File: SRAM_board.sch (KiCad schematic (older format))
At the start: 78 parts, among them J1 JP3, J10 Optional Interrupt Pins, J11 Optional Interrupt Pin, J12 GPIO 1, J13 GPIO 0, J14 USB_OTG, J2 JP6, J3 JP2, J4 JP5, J5 Screw_Terminal_01x09, J6 Screw_Terminal_01x06, J7 Optional I2C/UART, J9 Optional Interrupt Pin, SW1 KEY1, SW2 KEY0, U1 LD1085D2T33R, U2 MS561101BA03-50, U3 IIS2MDCTR, U4 GS832032AGT-150I, U5 BMI055, U6 ICM-20689, U7 FT232RL

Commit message: cleanup
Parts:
- removed unit 2 of U4
- removed unit 3 of U4
- removed unit 4 of U4
- removed unit 5 of U4
- removed unit 6 of U4
- added U? (x5): DE10_SRAM_expansion_GS832032AGT-150I-DE10_SRAM_ex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, symbol DE10_SRAM_expansion:DE10_SRAM_expansion_GS832032AGT-150I-DE10_SRAM_expansion
- U1: symbol SRAM_board-rescue:DE10_SRAM_expansion_LD1085D2T33R-DE10_SRAM_expansion -> DE10_SRAM_expansion:DE10_SRAM_expansion_LD1085D2T33R-DE10_SRAM_expansion
- U2: symbol SRAM_board-rescue:DE10_SRAM_expansion_MS561101BA03-50-DE10_SRAM_expansion -> DE10_SRAM_expansion:DE10_SRAM_expansion_MS561101BA03-50-DE10_SRAM_expansion
- U3: symbol SRAM_board-rescue:DE10_SRAM_expansion_IIS2MDCTR-DE10_SRAM_expansion -> DE10_SRAM_expansion:DE10_SRAM_expansion_IIS2MDCTR-DE10_SRAM_expansion
- U4: symbol SRAM_board-rescue:DE10_SRAM_expansion_GS832032AGT-150I-DE10_SRAM_expansion -> DE10_SRAM_expansion:DE10_SRAM_expansion_GS832032AGT-150I-DE10_SRAM_expansion
- U5: symbol SRAM_board-rescue:DE10_SRAM_expansion_BMI055-DE10_SRAM_expansion -> DE10_SRAM_expansion:DE10_SRAM_expansion_BMI055-DE10_SRAM_expansion
- U6: symbol SRAM_board-rescue:DE10_SRAM_expansion_ICM-20689-DE10_SRAM_expansion -> DE10_SRAM_expansion:DE10_SRAM_expansion_ICM-20689-DE10_SRAM_expansion
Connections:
- net A0: now also U?.37 (A0)
- net A1: now also U?.36 (A1)
- net A10: now also U?.43 (A)
- net A11: now also U?.45 (A)
- net A12: now also U?.47 (A)
- net A13: now also U?.48 (A)
- net A14: now also U?.49 (A)
- net A15: now also U?.50 (A)
- net A16: now also U?.81 (A)
- net A17: now also U?.82 (A)
- net A18: now also U?.99 (A)
- net A19: now also U?.100 (A)
- net A2: now also U?.32 (A)
- net A3: now also U?.33 (A)
- net A4: now also U?.34 (A)
- net A5: now also U?.35 (A)
- net A6: now also U?.39 (A)
- net A7: now also U?.44 (A)
- net A8: now also U?.42 (A)
- net A9: now also U?.46 (A)
- net CLK: now also U?.89 (CLK)
- net DQA1: now also U?.52 (DQA)
- net DQA2: now also U?.53 (DQA)
- net DQA3: now also U?.56 (DQA)
- net DQA4: now also U?.57 (DQA)
- net DQA5: now also U?.58 (DQA)
- net DQA6: now also U?.59 (DQA)
- net DQA7: now also U?.62 (DQA)
- net DQA8: now also U?.63 (DQA)
- net DQB1: now also U?.79 (DQB)
- net DQB2: now also U?.78 (DQB)
- net DQB3: now also U?.75 (DQB)
- net DQB4: now also U?.74 (DQB)
- net DQB5: now also U?.73 (DQB)
- net DQB6: now also U?.72 (DQB)
- net DQB7: now also U?.69 (DQB)
- net DQB8: now also U?.68 (DQB)
- net DQC1: now also U?.2 (DQC)
- net DQC2: now also U?.3 (DQC)
- net DQC3: now also U?.6 (DQC)
- net DQC4: now also U?.7 (DQC)
- net DQC5: now also U?.8 (DQC)
- net DQC6: now also U?.9 (DQC)
- net DQC7: now also U?.12 (DQC)
- net DQC8: now also U?.13 (DQC)
- net DQD1: now also U?.18 (DQD)
- net DQD2: now also U?.19 (DQD)
- net DQD3: now also U?.22 (DQD)
- net DQD4: now also U?.23 (DQD)
- net DQD5: now also U?.24 (DQD)
- net DQD6: now also U?.25 (DQD)
- net DQD7: now also U?.28 (DQD)
- net DQD8: now also U?.29 (DQD)
- net DQPA: now also U?.51 (DQPA)
- net DQPB: now also U?.80 (DQPB)
- net DQPC: now also U?.1 (DQPC)
- net DQPD: now also U?.30 (DQPD)
- net ZZ: now also U?.64 (ZZ)
- net ~ADSC: now also U?.85 (~ADSC)
- net ~ADSP: now also U?.84 (~ADSP)
- net ~ADV: now also U?.83 (~ADV)
- net ~BA: now also U?.93 (~BA)
- net ~BB: now also U?.94 (~BB)
- net ~BC: now also U?.95 (~BC)
- net ~BD: now also U?.96 (~BD)
- net ~BW: now also U?.87 (~BW)
- net ~E1: now also U?.98 (~E1)
- net ~E2: now also U?.97 (~E2)
- net ~E3: now also U?.92 (~E3)
- net ~FT: now also U?.14 (~FT)
- net ~G: now also U?.86 (~G)
- net ~GW: now also U?.88 (~GW)
- net ~LBO: now also U?.31 (~LBO)
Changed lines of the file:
@@
 EESchema Schematic File Version 4
-LIBS:SRAM_board-cache
 EELAYER 30 0
 EELAYER END
@@
 GP Buttons, Leds\n
 $Comp
-L SRAM_board-rescue:DE10_SRAM_expansion_BMI055-DE10_SRAM_expansion U5
+L DE10_SRAM_expansion:DE10_SRAM_expansion_BMI055-DE10_SRAM_expansion U5
 U 1 1 5DD1283D
 P 10400 7500
@@
 $EndComp
 $Comp
-L SRAM_board-rescue:DE10_SRAM_expansion_LD1085D2T33R-DE10_SRAM_expansion U1
+L DE10_SRAM_expansion:DE10_SRAM_expansion_LD1085D2T33R-DE10_SRAM_expansion U1
 U 1 1 5DD15E38
 P 4050 1850
@@
 $EndComp
 $Comp
-L SRAM_board-rescue:DE10_SRAM_expansion_GS832032AGT-150I-DE10_SRAM_expansion U4
+L DE10_SRAM_expansion:DE10_SRAM_expansion_GS832032AGT-150I-DE10_SRAM_expansion U4
 U 1 1 5DD17A72
 P 6000 4600
@@
 $EndComp
 $Comp
-L SRAM_board-rescue:DE10_SRAM_expansion_GS832032AGT-150I-DE10_SRAM_expansion U4
-U 2 1 5DD1E8B0
-P 18200 2150
-F 0 "U4" H 17900 2950 50  0000 C CNN
-F 1 "GS832032AGT-150I" H 18200 800 50  0000 C CNN
-F 2 "DE10_SRAM_board:PQFP-100_14x20mm_P0.65mm" H 17950 150 50  0001 C CNN
-F 3 "" H 17850 250 50  0001 C CNN
-	2    18200 2150
-	1    0    0    -1
-$EndComp
-$Comp
-L SRAM_board-rescue:DE10_SRAM_expansion_GS832032AGT-150I-DE10_SRAM_expansion U4
-U 3 1 5DD336C8
-P 14750 2000
-F 0 "U4" H 14650 2850 50  0000 L CNN
-F 1 "GS832032AGT-150I" H 14650 1650 50  0000 L CNN
-F 2 "DE10_SRAM_board:PQFP-100_14x20mm_P0.65mm" H 14500 0   50  0001 C CNN
-F 3 "" H 14400 100 50  0001 C CNN
-	3    14750 2000
-	1    0    0    -1
-$EndComp
-$Comp
-L SRAM_board-rescue:DE10_SRAM_expansion_GS832032AGT-150I-DE10_SRAM_expansion U4
-U 4 1 5DD38B2E
-P 9450 2000
-F 0 "U4" H 9650 2850 50  0000 L CNN
-F 1 "GS832032AGT-150I" H 8900 1650 50  0000 L CNN
-F 2 "DE10_SRAM_board:PQFP-100_14x20mm_P0.65mm" H 9200 0   50  0001 C CNN
-F 3 "" H 9100 100 50  0001 C CNN
-	4    9450 2000
-	-1   0    0    -1
-$EndComp
-$Comp
-L SRAM_board-rescue:DE10_SRAM_expansion_GS832032AGT-150I-DE10_SRAM_expansion U4
-U 5 1 5DD3B251
-P 14750 3350
-F 0 "U4" H 15050 4200 50  0000 C CNN
-F 1 "GS832032AGT-150I" H 14750 3100 50  0000 C CNN
-F 2 "DE10_SRAM_board:PQFP-100_14x20mm_P0.65mm" H 14500 1350 50  0001 C CNN
-F 3 "" H 14400 1450 50  0001 C CNN
-	5    14750 3350
-	1    0    0    -1
-$EndComp
-$Comp
-L SRAM_board-rescue:DE10_SRAM_expansion_GS832032AGT-150I-DE10_SRAM_expansion U4
-U 6 1 5DD3D3F0
-P 9450 3250
-F 0 "U4" H 9750 4100 50  0000 C CNN
-F 1 "GS832032AGT-150I" H 9450 3000 50  0000 C CNN
-F 2 "DE10_SRAM_board:PQFP-100_14x20mm_P0.65mm" H 9200 1250 50  0001 C CNN
-F 3 "" H 9100 1350 50  0001 C CNN
-	6    9450 3250
-	-1   0    0    -1
-$EndComp
-$Comp
-L SRAM_board-rescue:DE10_SRAM_expansion_MS561101BA03-50-DE10_SRAM_expansion U2
+L DE10_SRAM_expansion:DE10_SRAM_expansion_MS561101BA03-50-DE10_SRAM_expansion U2
 U 1 1 5DE27368
 P 5750 7600
@@
 $EndComp
 $Comp
-L SRAM_board-rescue:DE10_SRAM_expansion_IIS2MDCTR-DE10_SRAM_expansion U3
+L DE10_SRAM_expansion:DE10_SRAM_expansion_IIS2MDCTR-DE10_SRAM_expansion U3
 U 1 1 5DE29342
 P 5850 10600
@@
 $EndComp
 $Comp
-L SRAM_board-rescue:DE10_SRAM_expansion_ICM-20689-DE10_SRAM_expansion U6
+L DE10_SRAM_expansion:DE10_SRAM_expansion_ICM-20689-DE10_SRAM_expansion U6
 U 1 1 5DE2C4AF
 P 10900 10600
@@
 	17250 10650 17600 10650
 NoConn ~ 17600 10850
+$Comp
+L DE10_SRAM_expansion:DE10_SRAM_expansion_GS832032AGT-150I-DE10_SRAM_expansion U?
+U 4 1 5DEA11D4
+P 9450 2000
+F 0 "U?" H 9517 2965 50  0000 C CNN
+F 1 "DE10_SRAM_expansion_GS832032AGT-150I-DE10_SRAM_expansion" H 9517 2874 50  0000 C CNN
+F 2 "" H 9200 0   50  0001 C CNN
+F 3 "" H 9100 100 50  0001 C CNN
+	4    9450 2000
+	-1   0    0    -1
+$EndComp
+$Comp
+L DE10_SRAM_expansion:DE10_SRAM_expansion_GS832032AGT-150I-DE10_SRAM_expansion U?
+U 6 1 5DEA674C
+P 9450 3250
+F 0 "U?" H 9517 4215 50  0000 C CNN
+F 1 "DE10_SRAM_expansion_GS832032AGT-150I-DE10_SRAM_expansion" H 9517 4124 50  0000 C CNN
+F 2 "" H 9200 1250 50  0001 C CNN
+F 3 "" H 9100 1350 50  0001 C CNN
+	6    9450 3250
+	-1   0    0    -1
+$EndComp
+$Comp
+L DE10_SRAM_expansion:DE10_SRAM_expansion_GS832032AGT-150I-DE10_SRAM_expansion U?
+U 3 1 5DEABA45
+P 14750 2000
+F 0 "U?" H 15128 2296 50  0000 L CNN
+F 1 "DE10_SRAM_expansion_GS832032AGT-150I-DE10_SRAM_expansion" H 15128 2205 50  0000 L CNN
+F 2 "" H 14500 0   50  0001 C CNN
+F 3 "" H 14400 100 50  0001 C CNN
+	3    14750 2000
+	1    0    0    -1
+$EndComp
+$Comp
+L DE10_SRAM_expansion:DE10_SRAM_expansion_GS832032AGT-150I-DE10_SRAM_expansion U?
+U 5 1 5DEAFC8A
+P 14750 3350
+F 0 "U?" H 15128 3696 50  0000 L CNN
+F 1 "DE10_SRAM_expansion_GS832032AGT-150I-DE10_SRAM_expansion" H 15128 3605 50  0000 L CNN
+F 2 "" H 14500 1350 50  0001 C CNN
+F 3 "" H 14400 1450 50  0001 C CNN
+	5    14750 3350
+	1    0    0    -1
+$EndComp
+$Comp
+L DE10_SRAM_expansion:DE10_SRAM_expansion_GS832032AGT-150I-DE10_SRAM_expansion U?
+U 2 1 5DEB5E67
+P 18200 2150
+F 0 "U?" H 18175 3075 50  0000 C CNN
+F 1 "DE10_SRAM_expansion_GS832032AGT-150I-DE10_SRAM_expansion" H 18175 2984 50  0000 C CNN
+F 2 "" H 17950 150 50  0001 C CNN
+F 3 "" H 17850 250 50  0001 C CNN
+	2    18200 2150
+	1    0    0    -1
+$EndComp
 $EndSCHEMATC

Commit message: celanup, I2C improvment, SRAM clock buffer
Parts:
- added C38: 2.2uF, Capacitor_SMD:C_1206_3216Metric_Pad1.42x1.75mm_HandSolder, symbol Device:C_Small
- added C39: 100nF, Capacitor_SMD:C_1206_3216Metric_Pad1.42x1.75mm_HandSolder, symbol Device:C_Small
- added R14, R15, R16: 50R, Resistor_SMD:R_1206_3216Metric_Pad1.42x1.75mm_HandSolder, symbol Device:R_Small
- added U8: CDCLVC1102, DE10_SRAM_board:SOIC-8, symbol DE10_SRAM_expansion:CDCLVC1102
- U4: renamed from U?; value DE10_SRAM_expansion_GS832032AGT-150I-DE10_SRAM_expansion -> GS832032AGT-150I; footprint (none) -> DE10_SRAM_board:PQFP-100_14x20mm_P0.65mm
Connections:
- net +3V3: now also C38.1, C39.1, U8.6 (VDD)
- net CLK: now also R16.1; no longer J13.32 (Pin_32)
- net GND: now also C38.2, C39.2, R15.1, U8.2 (1G), U8.4 (GND)
- new net: R14.1, R15.2, U8.1 (CLKIN)
- new net: R16.2, U8.3 (Y0)
- new net CLK_IN: J13.32 (Pin_32), R14.2
- no-connect marks 21 -> 22
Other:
- note added: "CLOCK BUFFER"
- note added: "This makes the ERC happy\nStill host +5V power"
- note removed: "This makes the ERC happy\nStil host +5V power"
- moved on the sheet: J13, U4B

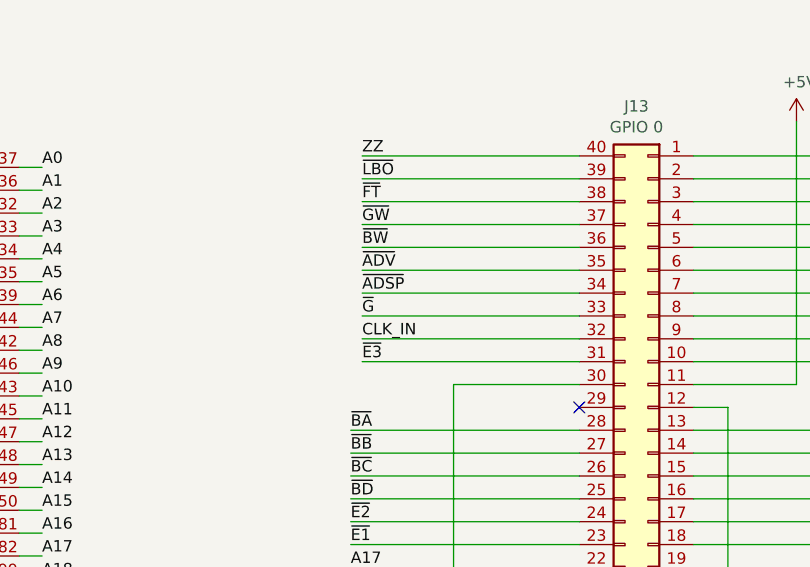
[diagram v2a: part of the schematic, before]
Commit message: switch sram clock pin
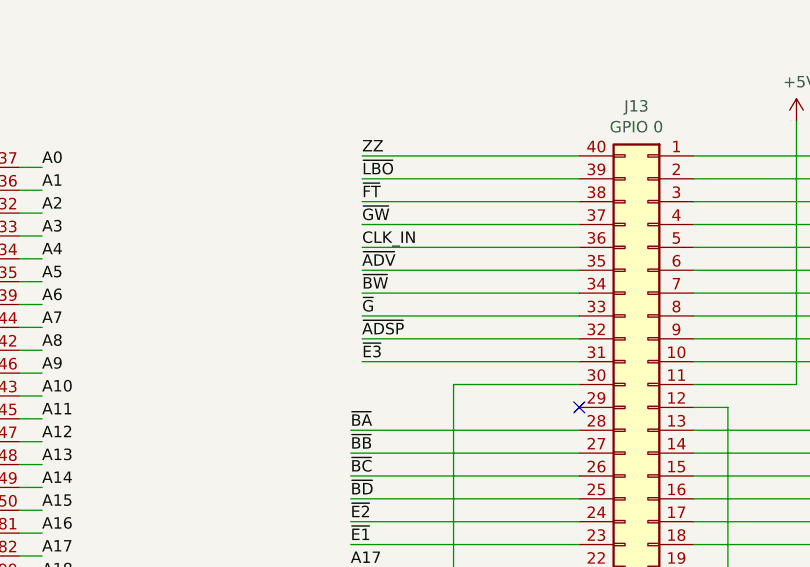
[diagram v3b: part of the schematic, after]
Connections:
- net CLK_IN: now also J13.36 (Pin_36); no longer J13.32 (Pin_32)
- net ~ADSP: now also J13.32 (Pin_32); no longer J13.34 (Pin_34)
- net ~BW: now also J13.34 (Pin_34); no longer J13.36 (Pin_36)
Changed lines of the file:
@@
 Text Label 19500 2350 0    50   ~ 0
 ~E3
-Text Label 19500 2250 0    50   ~ 0
+Text Label 19500 1850 0    50   ~ 0
 CLK_IN
 Text Label 19500 2150 0    50   ~ 0
 ~G
+Text Label 19500 2250 0    50   ~ 0
+~ADSP
 Text Label 19500 2050 0    50   ~ 0
-~ADSP
-Text Label 19500 1850 0    50   ~ 0
 ~BW
 Text Label 19500 1750 0    50   ~ 0
